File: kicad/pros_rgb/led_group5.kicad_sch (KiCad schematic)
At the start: 9 parts

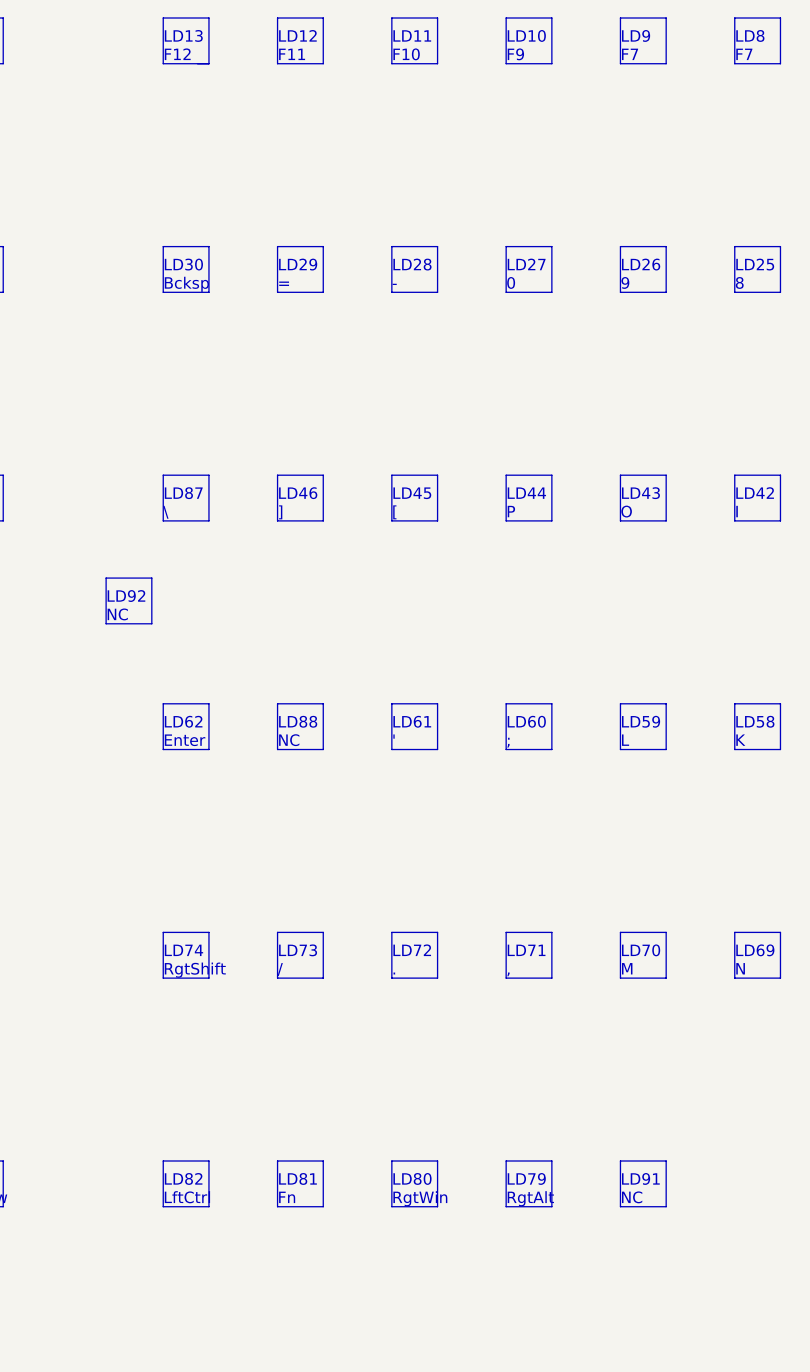
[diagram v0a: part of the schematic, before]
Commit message: kicad/pros_rgb: fix typos
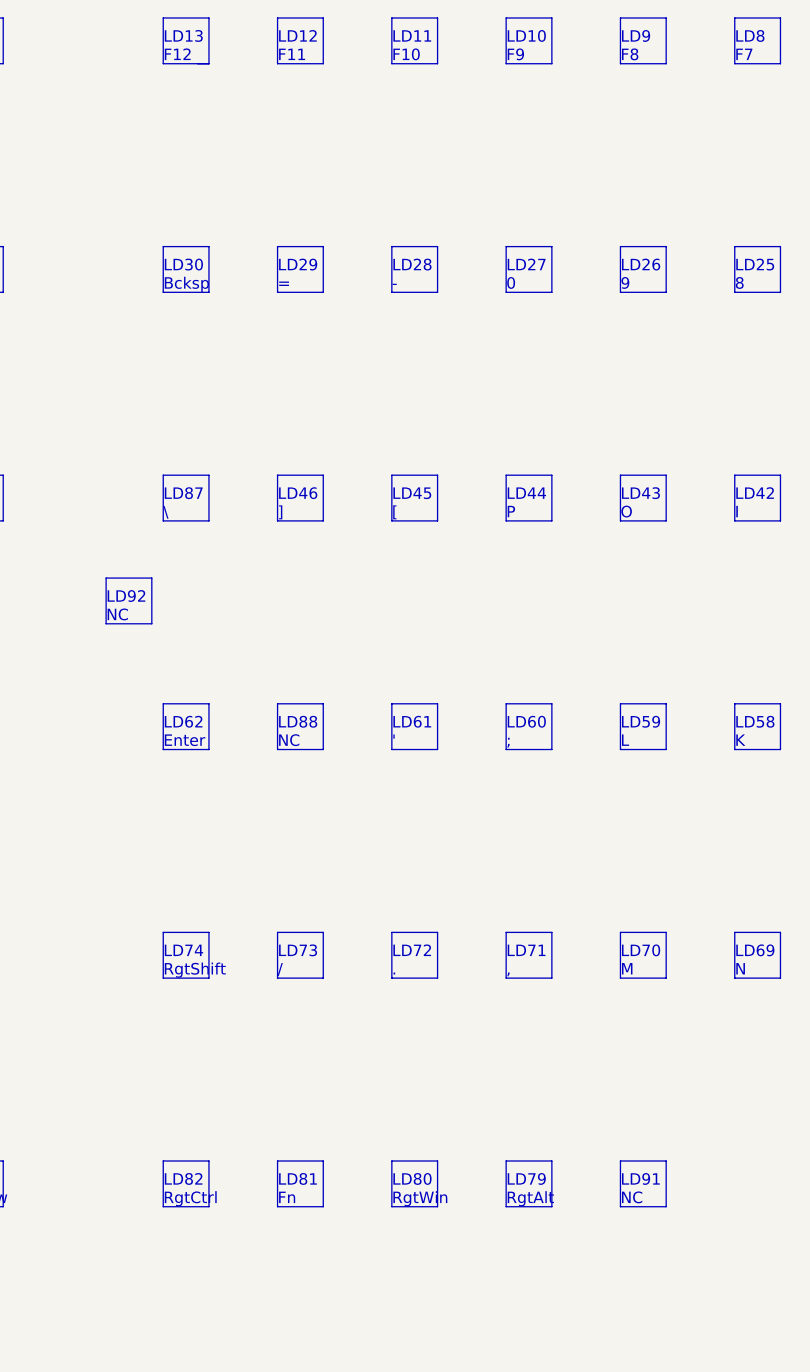
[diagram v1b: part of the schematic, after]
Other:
- note added: "LD82 RgtCtrl"
- note added: "LD9 F8"
- note removed: "LD82 LftCtrl"
- note removed: "LD9 F7"
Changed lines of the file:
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@@
     (effects (font (size 1.27 1.27)) (justify left bottom))
   )
-  (text "LD82\nLftCtrl" (at 106.68 156.21 0)
+  (text "LD82\nRgtCtrl" (at 106.68 156.21 0)
     (effects (font (size 1.27 1.27)) (justify left bottom))
   )
@@
     (effects (font (size 1.27 1.27)) (justify left bottom))
   )
-  (text "LD9\nF7" (at 157.48 29.21 0)
+  (text "LD9\nF8" (at 157.48 29.21 0)
     (effects (font (size 1.27 1.27)) (justify left bottom))
   )

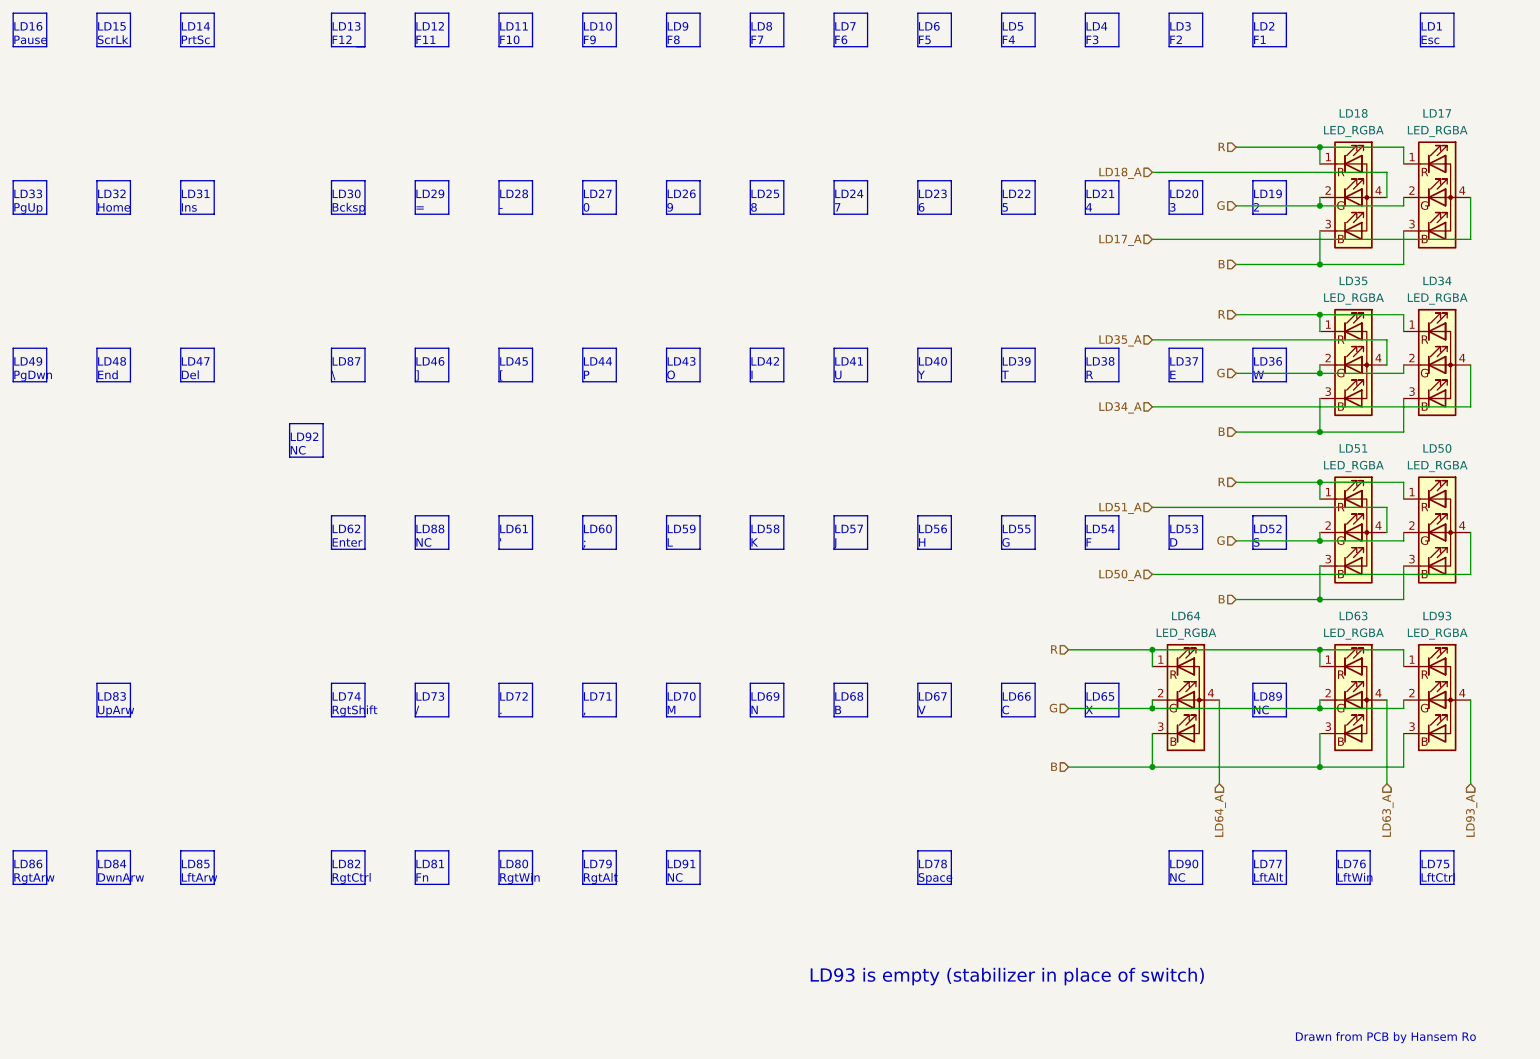
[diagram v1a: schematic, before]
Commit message: kicad/pros_rgb: order led groups by channel number
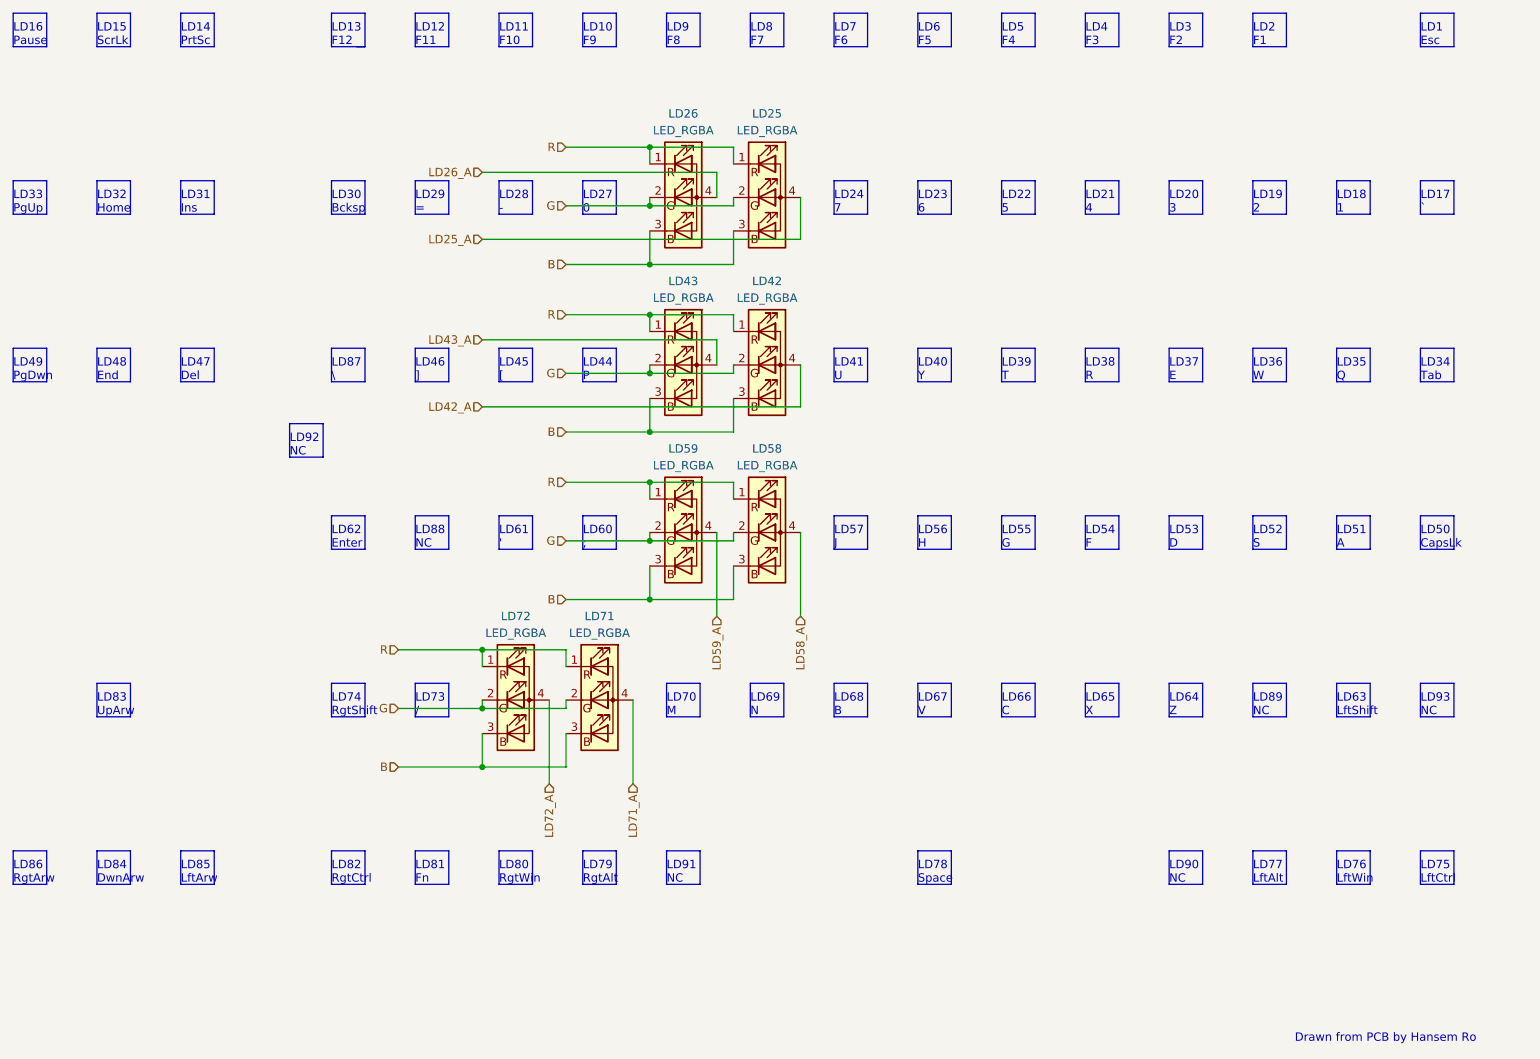
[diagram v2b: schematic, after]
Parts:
- removed LD17, LD18, LD34, LD35, LD50, LD51, LD63, LD64, LD93: LED_RGBA, symbol Device:LED_RGBA
- added LD25, LD26, LD42, LD43, LD58, LD59, LD71, LD72: LED_RGBA, symbol Device:LED_RGBA
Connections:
- net B: now also LD25.3 (BK), LD26.3 (BK), LD42.3 (BK), LD43.3 (BK), LD58.3 (BK), LD59.3 (BK), LD71.3 (BK), LD72.3 (BK)
- net G: now also LD25.2 (GK), LD26.2 (GK), LD42.2 (GK), LD43.2 (GK), LD58.2 (GK), LD59.2 (GK), LD71.2 (GK), LD72.2 (GK)
- net R: now also LD25.1 (RK), LD26.1 (RK), LD42.1 (RK), LD43.1 (RK), LD58.1 (RK), LD59.1 (RK), LD71.1 (RK), LD72.1 (RK)
- new net LD25_A: LD25.4 (A)
- new net LD26_A: LD26.4 (A)
- new net LD42_A: LD42.4 (A)
- new net LD43_A: LD43.4 (A)
- new net LD58_A: LD58.4 (A)
- new net LD59_A: LD59.4 (A)
- new net LD71_A: LD71.4 (A)
- new net LD72_A: LD72.4 (A)
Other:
- note added: "LD17 `"
- note added: "LD18 1"
- note added: "LD34 Tab"
- note added: "LD35 Q"
- note added: "LD50 CapsLk"
- note added: "LD51 A"
- note added: "LD63 LftShift"
- note added: "LD64 Z"
- note added: "LD93 NC"
- note removed: "LD25 8"
- note removed: "LD26 9"
- note removed: "LD42 I"
- note removed: "LD43 O"
- note removed: "LD58 K"
- note removed: "LD59 L"
- note removed: "LD71 ,"
- note removed: "LD72 ."
- note removed: "LD93 is empty (stabilizer in place of switch)"
